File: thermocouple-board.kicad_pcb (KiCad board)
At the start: 2 copper layers, 59.6 x 114.3 mm, 112 parts, among them J1 Programming Header, J10 TC7, J11 TC8, J2 RJ45_Amphenol_RJMG1BD3B8K1ANR, J3 Conn_01x02, J4 TC1, J5 TC2, J6 TC3, J7 TC4, J8 TC5, J9 TC6, SW1 RESET, U1 ATSAME51J20A-A, U10 ENC28J60x-SO, U11 MC33063AD, U2 MCP9601_ZM, U3 MCP9601_ZM, U4 MCP9601_ZM, U5 MCP9601_ZM, U6 MCP9601_ZM, U7 MCP9601_ZM, U8 MCP9601_ZM, U9 MCP9601_ZM, Y1 25MHz

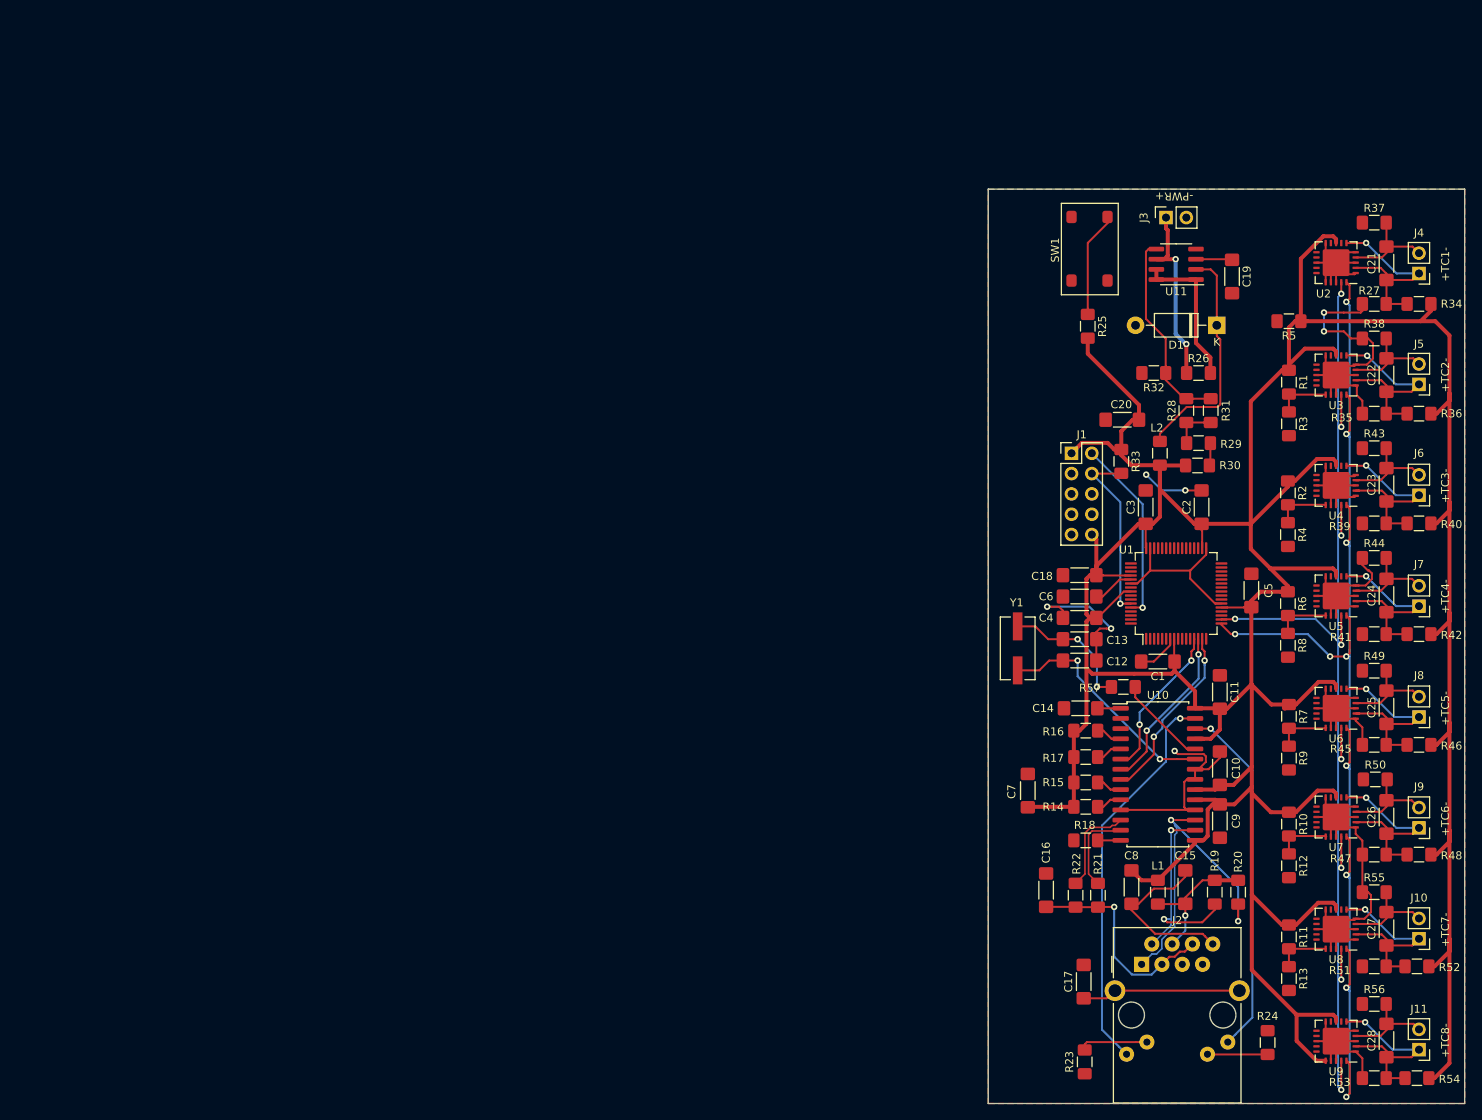
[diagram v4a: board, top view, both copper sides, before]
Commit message: Replace capacitor footprints with 1206
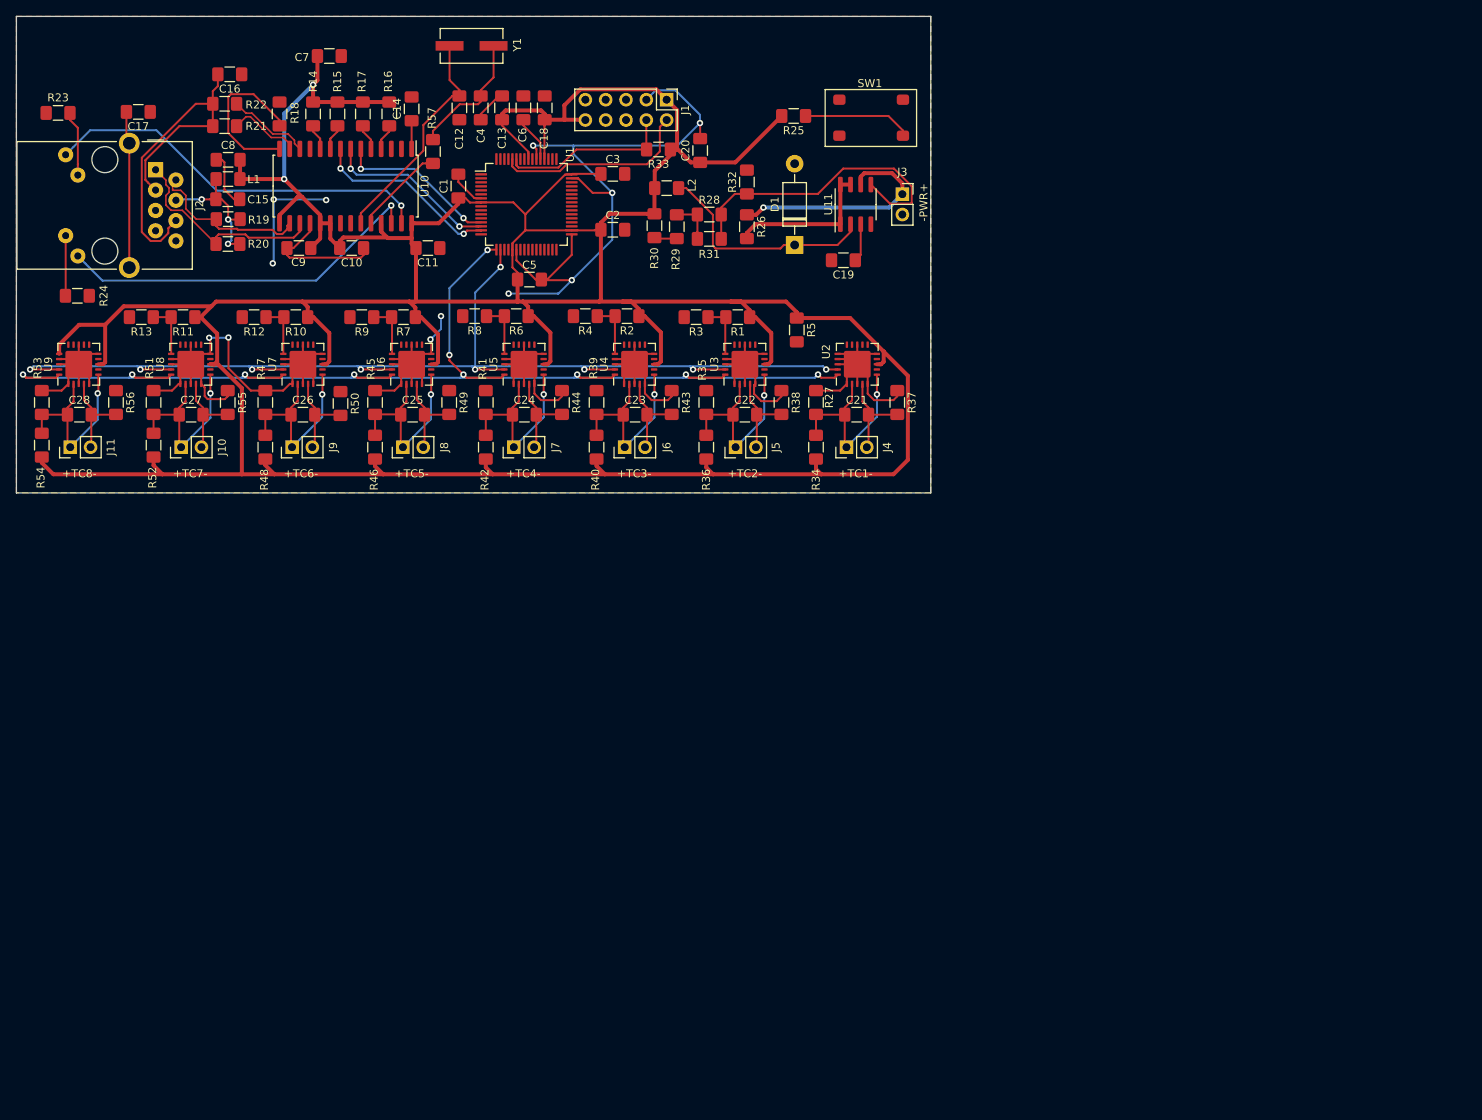
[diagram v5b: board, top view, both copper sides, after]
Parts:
- added QR*****: ID_QR_TC_PROTO_FEB_2020, thermocouple-board:ID_QR_TC_PROTO_FEB_2020, B.Cu at (163.5, 99.3)
- C1, C10, C11, C12, C13, C14, C15, C16, C17, C18, C19, C2, C20, C21, C22, C23, C24, C25, C26, C27, C28, C3, C4, C5, C6, C7, C8, C9: footprint Capacitor_SMD:C_1806_4516Metric_Pad1.57x1.80mm_HandSolder -> Capacitor_SMD:C_1206_3216Metric_Pad1.42x1.75mm_HandSolder
- R32: value 9K -> 10K
- moved R54 189.2 mm to (92.1, 118.1), turned to 270 degrees
- moved R53 186.7 mm to (92.1, 112.8), turned to 270 degrees
- moved J11 184.6 mm to (95.7, 118.4), turned to 90 degrees
- moved C28 181.1 mm to (96.8, 114.3), turned to 0 degrees
- moved U9 178.5 mm to (96.8, 108.0), turned to 90 degrees
- moved R24 175.6 mm to (96.6, 99.4), turned to 0 degrees
- moved R23 174.8 mm to (94.2, 76.6), turned to 180 degrees
- moved R56 174.3 mm to (101.4, 112.8), turned to 270 degrees
- moved R52 170.8 mm to (106.1, 118.1), turned to 270 degrees
- moved R51 168.1 mm to (106.1, 112.8), turned to 270 degrees
- moved J10 166.5 mm to (109.6, 118.4), turned to 90 degrees
- moved R13 165.6 mm to (104.6, 102.1), turned to 180 degrees
- moved C27 162.6 mm to (110.8, 114.3), turned to 0 degrees
- moved C17 160.6 mm to (104.2, 76.5), turned to 180 degrees
- moved U8 159.6 mm to (110.8, 108.0), turned to 90 degrees
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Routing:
- net GND: track 306.5 -> 357.8 mm, vias 7 -> 12
- net Net-(C16-Pad2): track 27.0 -> 48.3 mm, vias 1 -> 0
- net Net-(R18-Pad1): track 2.88 -> 20.4 mm
- net /Ethernet/TPOUT+: track 41.7 -> 26.6 mm, vias 2 -> 0
- net +3V3: track 543.7 -> 557.9 mm, vias 0 -> 2
- net Net-(R28-Pad2): track 25.1 -> 38.9 mm
- net /Ethernet/TPOUT-: track 27.3 -> 20.7 mm, vias 2 -> 0
- net VCC: track 23.7 -> 28.7 mm, vias 2 -> 1
- net /Ethernet/LEDB: track 44.6 -> 46.6 mm
- net /Ethernet/TPIN+: track 10.8 -> 9.16 mm
- net /Thermocouples/SDA: track 159.7 -> 161.2 mm
- net /MCU/SWDIO: track 23.4 -> 24.9 mm, vias 1 -> 0
- net /Ethernet/TPIN-: track 11.9 -> 10.5 mm
- net /Ethernet/SCK: track 22.7 -> 23.6 mm
- net /MCU/SWCLK: track 22.8 -> 21.8 mm, vias 1 -> 0
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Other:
- board size 59.6 x 114.3 mm -> 114.3 x 59.6 mm
- net class Power: trace_width 0.25 -> 0.5
